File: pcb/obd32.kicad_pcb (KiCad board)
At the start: 2 copper layers, 49.5 x 48.8 mm, 61 parts, among them J1 USB_C_Receptacle_USB2.0, J2 Micro_SD_Card, J3 OBD2, J4 67329-8040, J5 Conn_01x04_Female, SW1 SW_Push, SW2 SW_Push, SW3 SW_Push, U1 LMR33630BDDA, U2 ICM-20689, U3 AZ1117C-3.3, U4 ESP32-WROOM-32, U5 SiP32431DR3, U6 MCP2562-E-MF, U7 BMP280, U8 CP2102N-A01-GQFN24

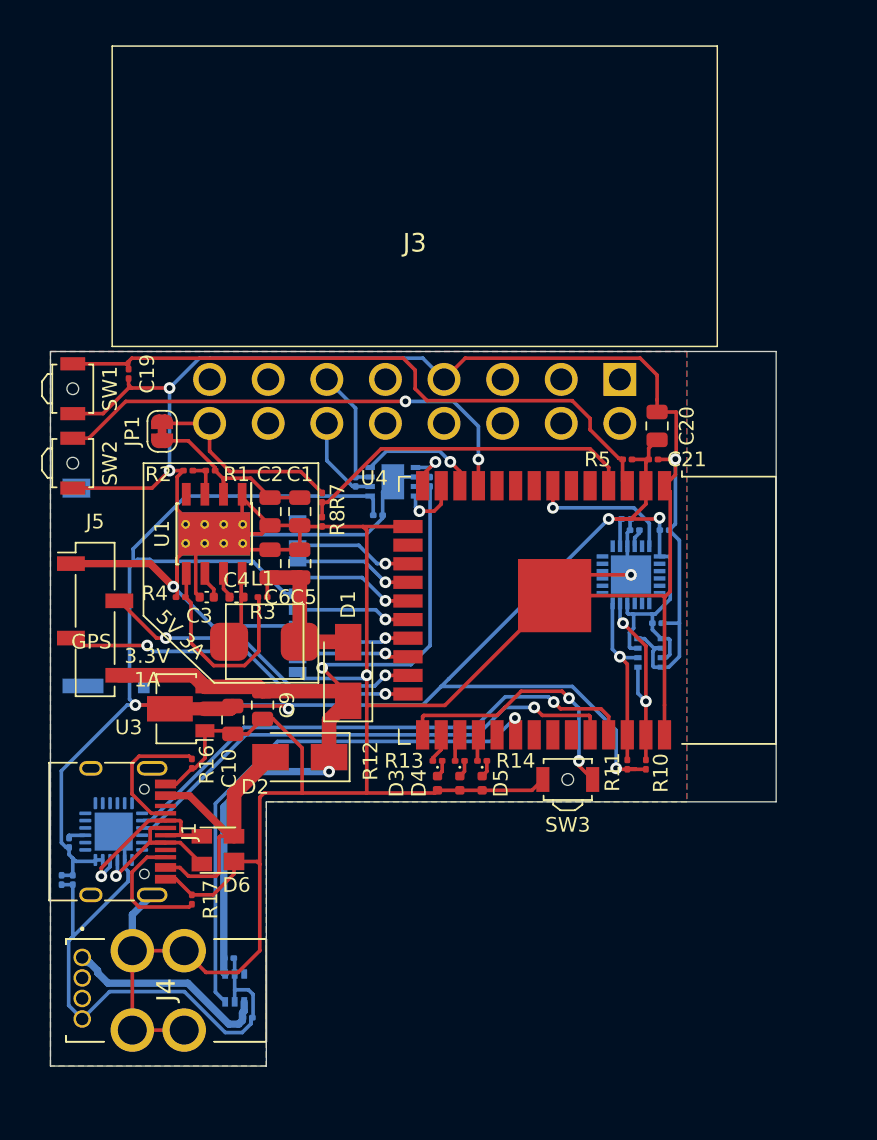
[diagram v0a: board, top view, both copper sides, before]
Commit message: PCB: Move components from bottom to top side of board. Move SD-card slot to sub board. Add SAM-M8N GPS-receiver
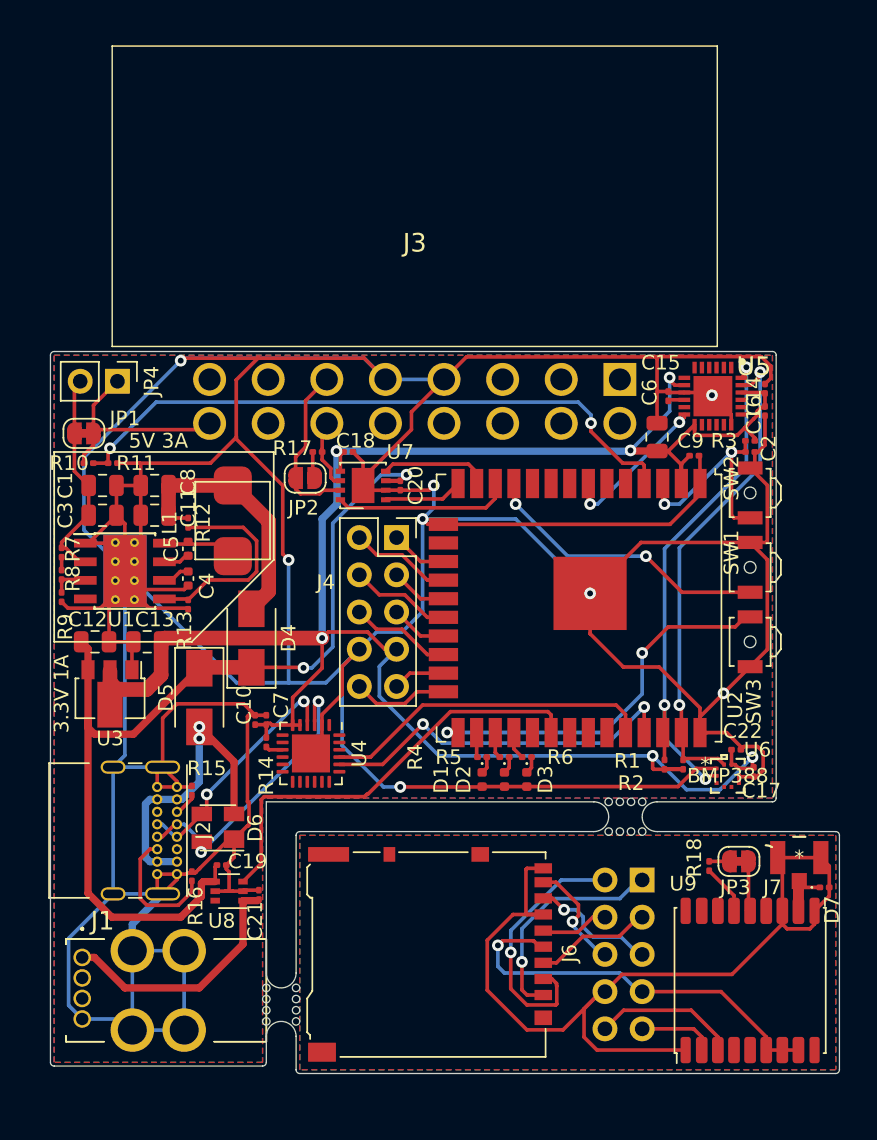
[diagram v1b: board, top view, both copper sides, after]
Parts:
- removed the C10 at (209.3, 87.4)
- removed the C15 at (236.2, 73.7)
- removed the C17 at (238.8, 74.4)
- removed the C6 at (211.8, 76.7)
- removed the C9 at (211.3, 86.4)
- removed the D1 at (217.2, 84.1)
- removed the R1 at (207.8, 70.4)
- removed the R3 at (211.3, 79.0)
- removed the R4 at (205.7, 79.0)
- removed the SW1 at (198.4, 64.8)
- removed the U2 at (236.5, 77.5)
- removed the U7 at (237.7, 82.8)
- added C12: 10µF, Capacitor_SMD:C_0805_2012Metric, F.Cu at (199.9, 82.0)
- added C13: 22µF, Capacitor_SMD:C_0805_2012Metric, F.Cu at (203.5, 82.0)
- added C14: 10nF, Capacitor_SMD:C_0201_0603Metric, F.Cu at (245.6, 64.8)
- added C16: 0.1µF, Capacitor_SMD:C_0201_0603Metric, F.Cu at (245.6, 66.3)
- added C22: 100nF, Capacitor_SMD:C_0201_0603Metric, F.Cu at (243.7, 89.4)
- added C8: 22µF, Capacitor_SMD:C_0805_2012Metric, F.Cu at (204.0, 71.4)
- added D4: D_Schottky, Diode_SMD:D_SMA, F.Cu at (210.6, 81.8)
- added D7: D_Zener, Diode_SMD:D_0201_0603Metric, F.Cu at (249.7, 98.8)
- added J6: Micro_SD_Card, Connector_Card:microSD_HC_Hirose_DM3AT-SF-PEJM5, F.Cu at (222.8, 103.4)
- added J7: U.FL-R-SMT-101, U.FL-R-SMT-101:U.FL-R-SMT-101, F.Cu at (248.0, 96.8)
- added JP2: SolderJumper_2_Open, Jumper:SolderJumper-2_P1.3mm_Open_RoundedPad1.0x1.5mm, F.Cu at (214.2, 70.9)
- added JP3: SolderJumper_2_Bridged, Jumper:SolderJumper-2_P1.3mm_Bridged_RoundedPad1.0x1.5mm, F.Cu at (243.8, 97.0)
- added JP4: Jumper_NO_Small, Connector_PinHeader_2.54mm:PinHeader_1x02_P2.54mm_Vertical, F.Cu at (201.4, 64.3)
- added R10: 100K, Resistor_SMD:R_0201_0603Metric, F.Cu at (199.5, 69.8)
- added R12: 100K, Resistor_SMD:R_0201_0603Metric, F.Cu at (206.2, 73.9)
- added R13: 24.9K, Resistor_SMD:R_0201_0603Metric, F.Cu at (206.2, 79.5)
- added R18: 10R, Resistor_SMD:R_0201_0603Metric, F.Cu at (241.8, 97.3)
- added R9: 100K, Resistor_SMD:R_0201_0603Metric, F.Cu at (197.6, 79.0)
- added SW2: SW_Push, Button_Switch_SMD:SW_SPST_B3U-3000P-B, F.Cu at (244.6, 71.9)
- added U6: BMP388, BMP388:BMP388, F.Cu at (243.1, 91.2)
- added U8: SiP32431DR3, Package_TO_SOT_SMD:SOT-363_SC-70-6, F.Cu at (209.0, 99.1)
- added U9: MAX-M8W, RF_GPS:ublox_MAX, F.Cu at (244.6, 105.2)
- C10: renamed from C8; moved to F.Cu
- C11: value 0.1µF -> 22µF; footprint Capacitor_SMD:C_0201_0603Metric -> Capacitor_SMD:C_0805_2012Metric; moved to F.Cu
- C15: renamed from C16; moved to F.Cu
- C17: renamed from C18; value 0.1µF -> 100nF; moved to F.Cu
- C18: renamed from C13; moved to F.Cu
- C19: value 1µF -> 0.1µF
- C2: value 220nF -> 1µF; footprint Capacitor_SMD:C_0805_2012Metric -> Capacitor_SMD:C_0201_0603Metric
- C20: renamed from C14; moved to F.Cu
- C21: renamed from C12; moved to F.Cu
- C3: value 1µF -> 220nF; footprint Capacitor_SMD:C_0402_1005Metric -> Capacitor_SMD:C_0805_2012Metric
- C4: value 0.1µF -> 1µF
- C5: value 22µF -> 0.1µF; footprint Capacitor_SMD:C_0805_2012Metric -> Capacitor_SMD:C_0402_1005Metric
- C7: moved to F.Cu
- J1: value USB_C_Receptacle_USB2.0 -> 67329-8040; footprint Connector_USB:USB_C_Receptacle_HRO_TYPE-C-31-M-12 -> 67329-8040:673298040
- J2: value Micro_SD_Card -> USB_C_Receptacle_USB2.0; footprint Connector_Card:microSD_HC_Hirose_DM3AT-SF-PEJM5 -> Connector_USB:USB_C_Receptacle_GCT_USB4085; moved to F.Cu
- J4: value 67329-8040 -> Conn_02x05_Odd_Even; footprint 67329-8040:673298040 -> Connector_PinSocket_2.54mm:PinSocket_2x05_P2.54mm_Vertical
- J5: value Conn_01x04_Female -> Conn_02x05_Odd_Even; footprint Connector_PinSocket_2.54mm:PinSocket_1x04_P2.54mm_Vertical_SMD_Pin1Left -> Connector_PinHeader_2.54mm:PinHeader_2x05_P2.54mm_Vertical; moved to B.Cu
- R11: value 4K7 -> 27K
- R14: renamed from R15; moved to F.Cu
- R17: renamed from R9; moved to F.Cu
- R2: value 100K -> 4K7
- R7: value 100K -> 10K
- R8: value 27K -> 866K
- U2: renamed from U4; footprint RF_Module:ESP32-WROOM-32 -> RF_Module:ESP32-WROOM-32U
- U4: renamed from U8; moved to F.Cu
- U5: value SiP32431DR3 -> ICM-20689; footprint Package_TO_SOT_SMD:SOT-363_SC-70-6 -> ICM-20689:QFN50P400X400X95-25N-D; moved to F.Cu
- U7: renamed from U6; moved to F.Cu
- moved U5 51.9 mm to (242.1, 65.3), turned to 270 degrees
- moved SW1 46.8 mm to (244.6, 77.0), turned to 270 degrees
- moved R11 41.8 mm to (201.1, 69.8), turned to 0 degrees
- moved J5 41.4 mm to (237.2, 98.3), turned to 180 degrees
- moved R2 39.3 mm to (240.0, 90.4), turned to 90 degrees
- moved J4 35.8 mm to (220.5, 74.9), turned to 0 degrees
- moved C19 34.1 mm to (208.5, 97.3), turned to 0 degrees
- moved C2 33.0 mm to (244.6, 69.1), turned to 180 degrees
- moved C11 30.6 mm to (204.0, 73.4), turned to 180 degrees
- moved R7 18.2 mm to (197.6, 75.9), turned to 90 degrees
- moved R8 18.1 mm to (197.6, 77.5)
- moved C7 17.7 mm to (211.6, 87.4), turned to 90 degrees
- moved C10 16.6 mm to (210.8, 87.4), turned to 90 degrees
- moved SW3 15.6 mm to (244.6, 82.0), turned to 270 degrees
- moved R14 15.1 mm to (211.6, 88.9), turned to 270 degrees
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- renumbered C20 to C6, C21 to C9, D3 to D1, D4 to D2, D5 to D3, D2 to D5, R10 to R1, R16 to R15, R17 to R16, R5 to R3, R12 to R4, R13 to R5, R14 to R6, SW2 to SW1
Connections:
- C11 pad 1: +5V -> Net-(C11-Pad1)
- C15 pad 2: Net-(C16-Pad2) -> Net-(C15-Pad2)
- C19 pad 1: GND -> +5V
- C19 pad 2: ESP32_EN -> GND
- C2 pad 2: Net-(C1-Pad1) -> ESP32_EN
- C3 pad 1: Net-(C3-Pad1) -> GND
- C3 pad 2: GND -> Net-(C1-Pad1)
- C4 pad 2: Net-(C4-Pad2) -> GND
- C5 pad 2: GND -> Net-(C5-Pad2)
- J3 pad 1: (no net) -> Net-(J3-Pad1)
- J3 pad 10: (no net) -> Net-(J3-Pad10)
- J3 pad 11: (no net) -> Net-(J3-Pad11)
- J3 pad 12: (no net) -> Net-(J3-Pad12)
- J3 pad 13: (no net) -> Net-(J3-Pad13)
- J3 pad 15: (no net) -> Net-(J3-Pad15)
- J3 pad 2: (no net) -> Net-(J3-Pad2)
- J3 pad 3: (no net) -> Net-(J3-Pad3)
- J3 pad 5: (no net) -> GND
- J3 pad 7: (no net) -> Net-(J3-Pad7)
- J3 pad 8: (no net) -> Net-(J3-Pad8)
- J3 pad 9: (no net) -> Net-(J3-Pad9)
- J4 pad 1: +5VP -> SD_DAT2
- J4 pad 2: (no net) -> SD_DAT3
- J4 pad 3: (no net) -> SD_CMD
- J4 pad 4: GND -> SD_CLK
- J5 pad 1: GND -> SD_DAT2_s
- J5 pad 2: GPS_RX -> SD_DAT3_s
- J5 pad 3: GPS_TX -> SD_CMD_s
- J5 pad 4: +5V -> SD_CLK_s
- L1 pad 1: Net-(C5-Pad1) -> Net-(C11-Pad1)
- L1 pad 2: Net-(C4-Pad2) -> Net-(C5-Pad2)
- R11 pad 1: +3V3 -> ADC
- R11 pad 2: I2C0_SCL -> GND
- R15 pad 2: Net-(J1-PadA5) -> Net-(J2-PadA5)
- R16 pad 1: Net-(J1-PadB5) -> Net-(J2-PadB5)
- R17 pad 1: CAN_H -> CAN_L
- R17 pad 2: CAN_L -> Net-(JP2-Pad2)
- R2 pad 1: Net-(R1-Pad2) -> +3V3
- R2 pad 2: GND -> I2C0_SCL
- R7 pad 1: +BATT -> Net-(R7-Pad1)
- R7 pad 2: ADC -> Net-(C1-Pad1)
- R8 pad 1: ADC -> Net-(R7-Pad1)
- R8 pad 2: GND -> Net-(R8-Pad2)
- U1 pad 3: Net-(R1-Pad2) -> Net-(R8-Pad2)
- U1 pad 4: (no net) -> Net-(U1-Pad4)
- U1 pad 6: Net-(C3-Pad1) -> Net-(C4-Pad1)
- U1 pad 7: Net-(C4-Pad1) -> Net-(C5-Pad1)
- U1 pad 8: Net-(C4-Pad2) -> Net-(C5-Pad2)
- U2 pad 10: (no net) -> Net-(U2-Pad10)
- U2 pad 16: (no net) -> Net-(U2-Pad16)
- U2 pad 29: (no net) -> Net-(U2-Pad29)
- U2 pad 31: (no net) -> Net-(U2-Pad31)
- U2 pad 32: (no net) -> Net-(U2-Pad32)
- U2 pad 33: (no net) -> Net-(U2-Pad33)
- U2 pad 5: (no net) -> Net-(U2-Pad5)
- U2 pad 6: (no net) -> Net-(U2-Pad6)
- U2 pad 8: (no net) -> Net-(U2-Pad8)
- U2 pad 9: (no net) -> Net-(U2-Pad9)
- U4 pad 1: (no net) -> Net-(U4-Pad1)
- U4 pad 10: (no net) -> Net-(U4-Pad10)
- U4 pad 11: (no net) -> Net-(U4-Pad11)
- U4 pad 12: (no net) -> Net-(U4-Pad12)
- U4 pad 13: (no net) -> Net-(U4-Pad13)
- U4 pad 14: (no net) -> Net-(U4-Pad14)
- U4 pad 15: (no net) -> Net-(U4-Pad15)
- U4 pad 16: (no net) -> Net-(U4-Pad16)
- U4 pad 17: (no net) -> Net-(U4-Pad17)
- U4 pad 18: (no net) -> Net-(U4-Pad18)
- U4 pad 19: (no net) -> Net-(U4-Pad19)
- U4 pad 22: (no net) -> Net-(U4-Pad22)
- U4 pad 23: (no net) -> Net-(U4-Pad23)
- U4 pad 24: (no net) -> Net-(U4-Pad24)
- U4 pad 7: (no net) -> Net-(U4-Pad7)
- U4 pad 8: (no net) -> Net-(U4-Pad8)
- U5 pad 1: +5VP -> Net-(U5-Pad1)
- U5 pad 2: GND -> Net-(U5-Pad2)
- U5 pad 3: USB_EN -> Net-(U5-Pad3)
- U5 pad 4: +5V -> Net-(U5-Pad4)
- U5 pad 5: GND -> Net-(U5-Pad5)
- U5 pad 6: (no net) -> Net-(U5-Pad6)
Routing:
- net GND: track 360.1 -> 467.6 mm, vias 6 -> 8
- net GND1: track 0.00 -> 62.5 mm
- net ESP32_EN: track 44.2 -> 14.9 mm, vias 0 -> 2
- net +3.3VA: track 0.00 -> 27.5 mm, vias 0 -> 1
- net I2C0_SDA: track 12.4 -> 37.1 mm, vias 1 -> 3
- net +3V3: track 159.7 -> 138.7 mm, vias 5 -> 6
- net I2C0_SCL: track 14.0 -> 33.7 mm
- net ADC: track 23.9 -> 43.5 mm, vias 0 -> 2
- net GPS_RX: track 22.4 -> 3.57 mm, vias 2 -> 0
- net GPS_TX: track 24.6 -> 6.56 mm, vias 2 -> 0
- net SD_DAT3_s: track 0.00 -> 17.9 mm, vias 0 -> 1
- net Net-(C11-Pad1): track 0.00 -> 17.7 mm
- net SD_DAT2_s: track 0.00 -> 14.9 mm, vias 0 -> 1
- net ESP32_MISC: track 33.5 -> 19.9 mm
- net UART_RX: track 35.4 -> 22.0 mm, vias 1 -> 0
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- added copper zone on B.Cu, net GND1
- added copper zone on F.Cu, net GND1
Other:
- board size 49.5 x 48.8 mm -> 53.8 x 49.3 mm
- board text removed: "GPS"

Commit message: Board: use different USB-C Receptable
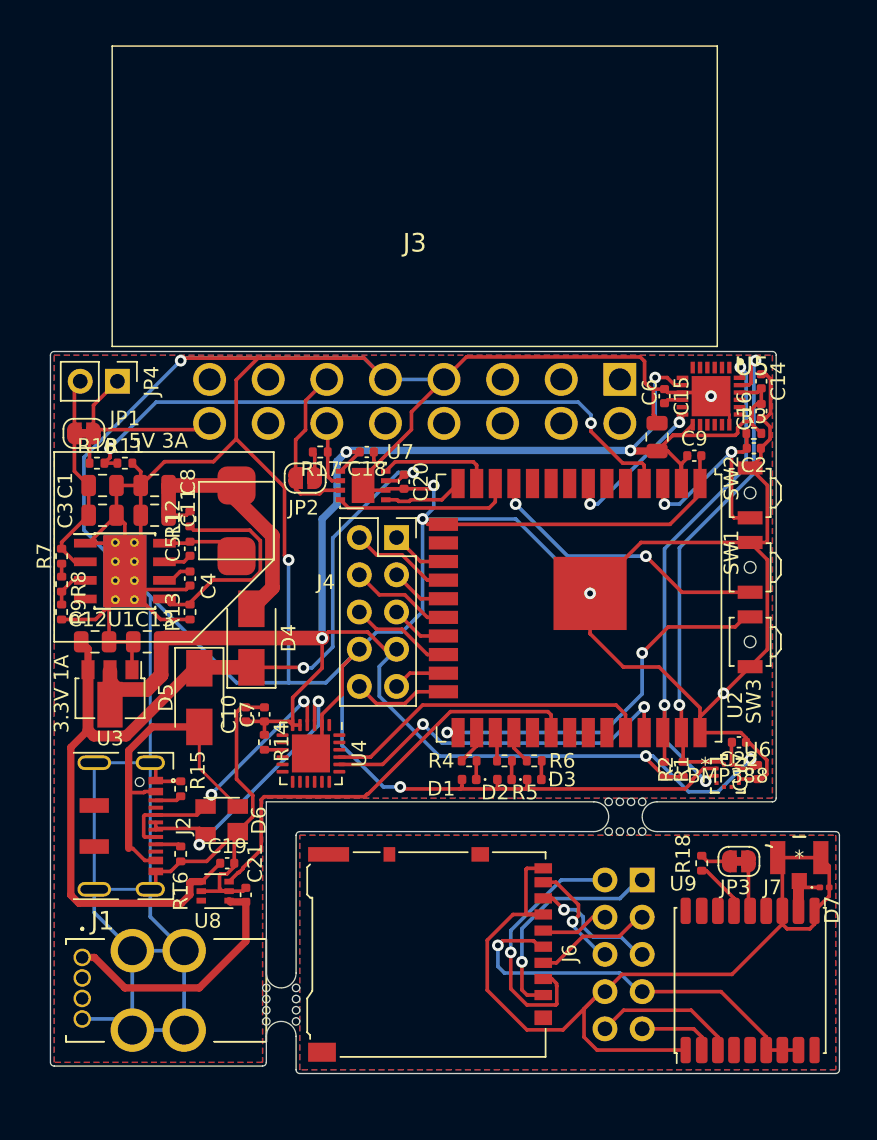
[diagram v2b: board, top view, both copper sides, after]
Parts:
- C10, C14, C15, C16, C17, C18, C19, C2, C20, C21, C22, C7, C9: footprint Capacitor_SMD:C_0201_0603Metric -> Capacitor_SMD:C_0402_1005Metric
- J2: footprint Connector_USB:USB_C_Receptacle_GCT_USB4085 -> USB_C_Receptacle_JAE_DX07S016JA1:USB_C_Receptacle_JAE_DX07S016JA1
- R1, R10, R11, R12, R13, R14, R15, R16, R17, R18, R2, R3, R4, R5, R6, R7, R8, R9: footprint Resistor_SMD:R_0201_0603Metric -> Resistor_SMD:R_0402_1005Metric
- moved J2 4.65 mm to (201.7, 94.6)
- moved R16 1.70 mm to (205.7, 96.5), turned to 270 degrees
- moved C18 1.27 mm to (218.4, 69.1)
- moved R9 1.02 mm to (197.6, 80.0)
- moved U8 0.95 mm to (208.1, 99.1)
- moved R4 0.92 mm to (225.4, 90.2)
- moved C21 0.89 mm to (210.2, 99.3)
- moved D1 0.89 mm to (225.4, 91.4), turned to 180 degrees
- moved R11 0.83 mm to (201.9, 69.8)
- moved R15 0.77 mm to (205.7, 92.1)
- moved C10 0.74 mm to (210.2, 87.0)
- moved R8 0.64 mm to (197.6, 78.1)
- moved R10 0.57 mm to (200.0, 69.8)
- moved R6 0.57 mm to (229.9, 90.2)
- moved D6 0.57 mm to (208.5, 94.2)
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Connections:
- J1 pad 2: Net-(J1-Pad2) -> (no net)
- J1 pad 3: Net-(J1-Pad3) -> (no net)
- J2 pad A8: Net-(J2-PadA8) -> (no net)
- J2 pad B8: Net-(J2-PadB8) -> (no net)
- J3 pad 1: Net-(J3-Pad1) -> (no net)
- J3 pad 10: Net-(J3-Pad10) -> (no net)
- J3 pad 11: Net-(J3-Pad11) -> (no net)
- J3 pad 12: Net-(J3-Pad12) -> (no net)
- J3 pad 13: Net-(J3-Pad13) -> (no net)
- J3 pad 15: Net-(J3-Pad15) -> (no net)
- J3 pad 2: Net-(J3-Pad2) -> (no net)
- J3 pad 3: Net-(J3-Pad3) -> (no net)
- J3 pad 7: Net-(J3-Pad7) -> (no net)
- J3 pad 8: Net-(J3-Pad8) -> (no net)
- J3 pad 9: Net-(J3-Pad9) -> (no net)
- U1 pad 4: Net-(U1-Pad4) -> (no net)
- U2 pad 10: Net-(U2-Pad10) -> (no net)
- U2 pad 16: Net-(U2-Pad16) -> (no net)
- U2 pad 29: Net-(U2-Pad29) -> (no net)
- U2 pad 31: Net-(U2-Pad31) -> (no net)
- U2 pad 32: Net-(U2-Pad32) -> (no net)
- U2 pad 33: Net-(U2-Pad33) -> (no net)
- U2 pad 5: Net-(U2-Pad5) -> (no net)
- U2 pad 6: Net-(U2-Pad6) -> (no net)
- U2 pad 8: Net-(U2-Pad8) -> (no net)
- U2 pad 9: Net-(U2-Pad9) -> (no net)
- U4 pad 1: Net-(U4-Pad1) -> (no net)
- U4 pad 10: Net-(U4-Pad10) -> (no net)
- U4 pad 11: Net-(U4-Pad11) -> (no net)
- U4 pad 12: Net-(U4-Pad12) -> (no net)
- U4 pad 13: Net-(U4-Pad13) -> (no net)
- U4 pad 14: Net-(U4-Pad14) -> (no net)
- U4 pad 15: Net-(U4-Pad15) -> (no net)
- U4 pad 16: Net-(U4-Pad16) -> (no net)
- U4 pad 17: Net-(U4-Pad17) -> (no net)
- U4 pad 18: Net-(U4-Pad18) -> (no net)
- U4 pad 19: Net-(U4-Pad19) -> (no net)
- U4 pad 22: Net-(U4-Pad22) -> (no net)
- U4 pad 23: Net-(U4-Pad23) -> (no net)
- U4 pad 24: Net-(U4-Pad24) -> (no net)
- U4 pad 7: Net-(U4-Pad7) -> (no net)
- U4 pad 8: Net-(U4-Pad8) -> (no net)
- U5 pad 1: Net-(U5-Pad1) -> (no net)
- U5 pad 11: Net-(U5-Pad11) -> (no net)
- U5 pad 14: Net-(U5-Pad14) -> (no net)
- U5 pad 15: Net-(U5-Pad15) -> (no net)
- U5 pad 16: Net-(U5-Pad16) -> (no net)
- U5 pad 17: Net-(U5-Pad17) -> (no net)
- U5 pad 19: Net-(U5-Pad19) -> (no net)
- U5 pad 2: Net-(U5-Pad2) -> (no net)
- U5 pad 20: Net-(U5-Pad20) -> (no net)
- U5 pad 21: Net-(U5-Pad21) -> (no net)
- U5 pad 3: Net-(U5-Pad3) -> (no net)
- U5 pad 4: Net-(U5-Pad4) -> (no net)
- U5 pad 5: Net-(U5-Pad5) -> (no net)
- U5 pad 6: Net-(U5-Pad6) -> (no net)
- U5 pad 7: Net-(U5-Pad7) -> (no net)
- U6 pad 5: Net-(U6-Pad5) -> (no net)
- U6 pad 6: Net-(U6-Pad6) -> (no net)
- U6 pad 7: Net-(U6-Pad7) -> (no net)
- U8 pad 6: Net-(U8-Pad6) -> (no net)
- U9 pad 13: Net-(U9-Pad13) -> (no net)
- U9 pad 16: Net-(U9-Pad16) -> (no net)
- U9 pad 17: Net-(U9-Pad17) -> (no net)
- U9 pad 18: Net-(U9-Pad18) -> (no net)
- U9 pad 4: Net-(U9-Pad4) -> (no net)
- U9 pad 5: Net-(U9-Pad5) -> (no net)
- U9 pad 9: Net-(U9-Pad9) -> (no net)
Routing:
- net GND: track 467.6 -> 455.8 mm
- net Net-(J2-PadB5): track 8.97 -> 1.76 mm
- net +3V3: track 138.7 -> 140.9 mm
- net +5VA: track 20.9 -> 22.8 mm, vias 2 -> 0
- net I2C0_SCL: track 33.7 -> 35.0 mm
- net USB_D-: track 16.2 -> 17.6 mm
- net Net-(R12-Pad1): track 14.3 -> 15.0 mm
- net ESP32_EN: track 14.9 -> 15.6 mm
- net Net-(JP3-Pad1): track 1.38 -> 2.05 mm
- net Net-(C11-Pad1): track 17.7 -> 18.3 mm

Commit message: Board: Adjustments
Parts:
- removed JP1: SolderJumper_2_Bridged, Jumper:SolderJumper-2_P1.3mm_Bridged_RoundedPad1.0x1.5mm
- removed JP4: Jumper_NO_Small, Connector_PinHeader_2.54mm:PinHeader_1x02_P2.54mm_Vertical
- removed L1: 2.2µH, TDK_SPM5030:TDK_SPM5030
- removed R7: 10K, Resistor_SMD:R_0402_1005Metric
- removed R8: 866K, Resistor_SMD:R_0402_1005Metric
- removed R9: 100K, Resistor_SMD:R_0402_1005Metric
- added C25: 22uF, Capacitor_SMD:C_0805_2012Metric, F.Cu at (206.0, 72.6)
- added D8: D_Schottky, Diode_SMD:D_SMA, F.Cu at (212.1, 81.9)
- added F1: Polyfuse, Fuse:Fuse_1812_4532Metric_Castellated, F.Cu at (204.0, 66.0)
- added J8: Conn_01x04_Male, Connector_PinHeader_2.54mm:PinHeader_1x04_P2.54mm_Vertical, F.Cu at (236.2, 94.0)
- added J9: Conn_01x04_Male, Connector_PinHeader_2.54mm:PinHeader_1x04_P2.54mm_Vertical, F.Cu at (221.0, 94.0)
- added L2: 3.3uH 4A 16mR, TDK_SPM5030:TDK_SPM5030, F.Cu at (205.7, 73.7)
- added Q1: BC817, Package_TO_SOT_SMD:SOT-23, F.Cu at (216.9, 90.4)
- added Q2: BC817, Package_TO_SOT_SMD:SOT-23, F.Cu at (220.5, 90.4)
- added R19: 27R, Resistor_SMD:R_0402_1005Metric, F.Cu at (207.5, 90.4)
- added R21: 100K, Resistor_SMD:R_0402_1005Metric, F.Cu at (207.3, 78.0)
- added R22: 24.9K, Resistor_SMD:R_0402_1005Metric, F.Cu at (206.2, 80.0)
- added R23: 10K, Resistor_SMD:R_0402_1005Metric, F.Cu at (215.9, 87.9)
- added R24: 10K, Resistor_SMD:R_0402_1005Metric, F.Cu at (218.9, 87.9)
- added REF**: OSHW-Logo2_9.8x8mm_SilkScreen, Symbol:OSHW-Logo2_9.8x8mm_SilkScreen, B.Cu at (232.4, 82.8)
- C1: value 10µF -> 100nF
- C10: value 0.1µF -> 1uF
- C11: value 22µF -> 0.1uF; footprint Capacitor_SMD:C_0805_2012Metric -> Capacitor_SMD:C_0402_1005Metric
- C12: value 10µF -> 22uF
- C13: value 22µF -> 22uF
- C15: value 0.47µF -> 0.47uF
- C16, C18, C19, C20, C21, C9: value 0.1µF -> 0.1uF
- C2: value 1µF -> 1uF
- C3: value 220nF -> 100nF
- C4: value 1µF -> 10uF; footprint Capacitor_SMD:C_0402_1005Metric -> Capacitor_SMD:C_0805_2012Metric
- C5: value 0.1µF -> 22uF; footprint Capacitor_SMD:C_0402_1005Metric -> Capacitor_SMD:C_0805_2012Metric
- C6: value 10µF -> 10uF
- C7: value 4.7µF -> 10uF 20V; footprint Capacitor_SMD:C_0402_1005Metric -> Capacitor_SMD:C_0805_2012Metric
- C8: value 22µF -> 220nF 20V; footprint Capacitor_SMD:C_0805_2012Metric -> Capacitor_SMD:C_0402_1005Metric
- D4: value D_Schottky -> SM6T18A; footprint Diode_SMD:D_SMA -> Diode_SMD:D_SMB
- R1, R2: footprint Resistor_SMD:R_0402_1005Metric -> Resistor_SMD:R_0603_1608Metric
- R12: value 100K -> 200K
- R13: value 24.9K -> 22K
- R14: value 1K -> 5.1K
- R16: value 5.1K -> 27R
- R4, R5: value 65R -> 64.9R
- R6: value 5R -> 4.99R
- U1: value LMR33630BDDA -> FT231XQ; footprint Package_SO:Texas_HSOP-8-1EP_3.9x4.9mm_P1.27mm_ThermalVias -> Package_DFN_QFN:QFN-20-1EP_4x4mm_P0.5mm_EP2.5x2.5mm
- U4: value CP2102N-A01-GQFN24 -> LMR33640DDDA; footprint Package_DFN_QFN:QFN-24-1EP_4x4mm_P0.5mm_EP2.6x2.6mm -> Package_SO:Texas_HSOP-8-1EP_3.9x4.9mm_P1.27mm_ThermalVias
- U7: value MCP2562-E-MF -> MCP2562FD-E-MF
- moved R10 33.0 mm to (233.0, 69.2)
- moved R11 33.0 mm to (234.9, 69.2)
- moved C1 24.8 mm to (210.6, 94.0), turned to 90 degrees
- moved C3 22.1 mm to (208.5, 94.0), turned to 270 degrees
- moved D4 19.6 mm to (199.6, 65.5)
- moved C7 19.3 mm to (198.9, 72.4), turned to 0 degrees
- moved U4 17.8 mm to (201.9, 77.2), turned to 0 degrees
- moved U1 14.9 mm to (211.8, 88.4), turned to 270 degrees
- moved D5 12.0 mm to (214.0, 76.1), turned to 90 degrees
- moved C10 9.84 mm to (206.2, 78.0), turned to 270 degrees
- moved C12 9.62 mm to (201.9, 72.6), turned to 270 degrees
- moved C13 9.41 mm to (204.0, 72.6), turned to 270 degrees
- moved R12 9.36 mm to (197.6, 77.0)
- moved R13 8.82 mm to (197.6, 79.0), turned to 270 degrees
- moved C4 7.65 mm to (199.9, 81.8), turned to 0 degrees
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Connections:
- C1 pad 1: Net-(C1-Pad1) -> GND
- C1 pad 2: GND -> +5VA
- C10 pad 1: +3V3 -> Net-(C10-Pad1)
- C11 pad 2: GND -> Net-(C11-Pad2)
- C12 pad 1: +5V -> Net-(C12-Pad1)
- C13 pad 1: +3V3 -> Net-(C12-Pad1)
- C3 pad 1: GND -> Net-(C3-Pad1)
- C3 pad 2: Net-(C1-Pad1) -> GND
- C4 pad 1: Net-(C4-Pad1) -> +5V
- C5 pad 1: Net-(C5-Pad1) -> +3V3
- C5 pad 2: Net-(C5-Pad2) -> GND
- C7 pad 1: +3V3 -> Net-(C7-Pad1)
- C8 pad 1: Net-(C11-Pad1) -> Net-(C7-Pad1)
- D4 pad 1: +5V -> Net-(C7-Pad1)
- D4 pad 2: Net-(C11-Pad1) -> GND
- D5 pad 2: +5VA -> Net-(C12-Pad1)
- D6 pad 3: USB_D- -> Net-(D6-Pad3)
- D6 pad 4: USB_D+ -> Net-(D6-Pad4)
- J2 pad A6: USB_D+ -> Net-(D6-Pad4)
- J2 pad A7: USB_D- -> Net-(D6-Pad3)
- J2 pad B6: USB_D+ -> Net-(D6-Pad4)
- J2 pad B7: USB_D- -> Net-(D6-Pad3)
- R12 pad 2: Net-(C11-Pad1) -> Net-(C7-Pad1)
- R13 pad 1: GND -> Net-(R12-Pad1)
- R13 pad 2: Net-(R12-Pad1) -> GND
- R14 pad 1: +3V3 -> GND
- R14 pad 2: Net-(R14-Pad2) -> Net-(J2-PadA5)
- R15 pad 1: GND -> Net-(J2-PadB5)
- R15 pad 2: Net-(J2-PadA5) -> GND
- R16 pad 1: Net-(J2-PadB5) -> Net-(D6-Pad3)
- R16 pad 2: GND -> USB_D-
- U1 pad 1: GND -> UART_TX
- U1 pad 2: Net-(C1-Pad1) -> (no net)
- U1 pad 3: Net-(R8-Pad2) -> GND
- U1 pad 5: Net-(R12-Pad1) -> (no net)
- U1 pad 6: Net-(C4-Pad1) -> (no net)
- U1 pad 7: Net-(C5-Pad1) -> (no net)
- U1 pad 8: Net-(C5-Pad2) -> USB_D+
- U1 pad 9: GND -> USB_D-
- U4 pad 1: (no net) -> GND
- U4 pad 2: GND -> Net-(C7-Pad1)
- U4 pad 3: USB_D+ -> Net-(R12-Pad1)
- U4 pad 4: USB_D- -> (no net)
- U4 pad 5: +3V3 -> Net-(R21-Pad1)
- U4 pad 6: +3V3 -> Net-(C10-Pad1)
- U4 pad 7: (no net) -> Net-(C11-Pad1)
- U4 pad 8: (no net) -> Net-(C11-Pad2)
- U4 pad 9: Net-(R14-Pad2) -> GND
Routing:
- net ADC: track 43.7 -> 5.39 mm, vias 2 -> 0
- net ESP32_EN: track 15.6 -> 46.6 mm, vias 2 -> 5
- net UART_RX: track 22.0 -> 48.3 mm, vias 0 -> 2
- net UART_TX: track 24.7 -> 49.3 mm
- net Net-(C12-Pad1): track 0.00 -> 21.7 mm
- net +BATT: track 14.6 -> 32.9 mm, vias 0 -> 1
- net USB_D+: track 19.9 -> 3.16 mm, vias 2 -> 0
- net Net-(C11-Pad1): track 18.3 -> 1.68 mm
- net Net-(C7-Pad1): track 0.00 -> 15.8 mm
- net /USB-to-Serial/DTR: track 0.00 -> 15.4 mm
- net /USB-to-Serial/RTS: track 0.00 -> 15.2 mm, vias 0 -> 2
- net Net-(C1-Pad1): track 14.7 -> 0.00 mm
- net Net-(D6-Pad3): track 0.00 -> 14.6 mm, vias 0 -> 2
- net USB_D-: track 17.6 -> 3.59 mm, vias 2 -> 0
- net Net-(R12-Pad1): track 15.0 -> 2.68 mm
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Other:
- board size 53.8 x 49.3 mm -> 53.8 x 53.1 mm
- board text added: "5V 4A"
- board text added: "OBD32"
- board text added: "by Malte Schröder"
- board text removed: "5V 3A"
